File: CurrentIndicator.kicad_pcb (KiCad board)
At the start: 2 copper layers, 60 x 100 mm, 79 parts, among them J1 Conn_01x02_Male, J2 Conn_01x04_Male, J3 Conn_01x04_Male, J6 Micro_SD_Card_Det, J7 USB_B_Micro, Q1 IRLML6344TRPBFTR, Q2 IRLML6344TRPBFTR, Q3 IRLML6344TRPBFTR, Q4 IRLML6344TRPBFTR, SW1 TVAF06-A020B-R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

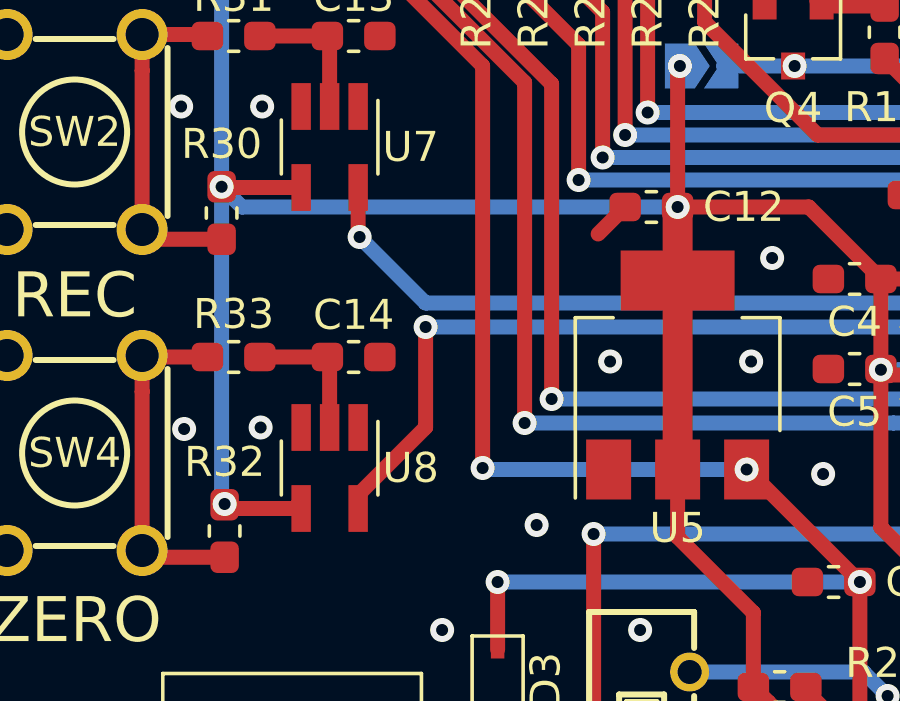
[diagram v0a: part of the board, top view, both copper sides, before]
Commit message: シュミットトリガのピン配置修正
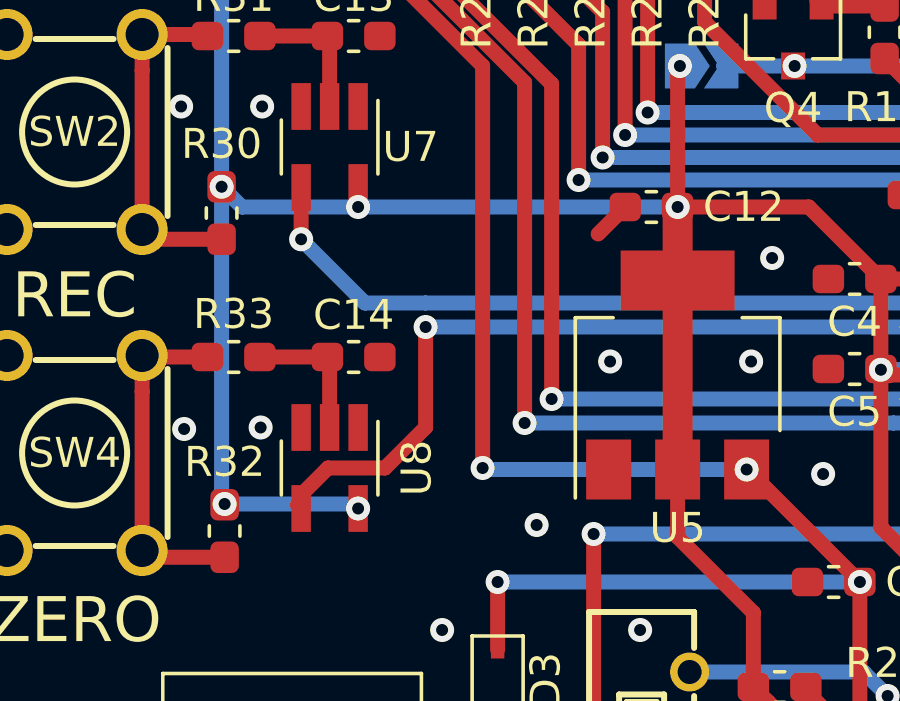
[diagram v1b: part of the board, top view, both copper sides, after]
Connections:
- U7 pad 4: +3V3 -> /REC_SW
- U7 pad 5: /REC_SW -> +3V3
- U8 pad 4: +3V3 -> /OFFSET_SW
- U8 pad 5: /OFFSET_SW -> +3V3
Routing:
- net /OFFSET_SW: track 25.6 -> 27.7 mm
- net /REC_SW: track 23.4 -> 25.4 mm
- net +3V3: track 225.5 -> 225.9 mm, vias 9 -> 11
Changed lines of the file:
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@@
     (thickness 1.6)
     (drawings 28)
-    (tracks 456)
+    (tracks 463)
     (zones 0)
     (modules 79)
@@
   )
   (setup
-    (last_trace_width 0.25)
+    (last_trace_width 0.5)
     (user_trace_width 0.5)
     (user_trace_width 1)
@@
     (add_net "Net-(J6-Pad11)")
     (add_net "Net-(J6-Pad8)")
+    (add_net "Net-(J7-Pad4)")
     (add_net "Net-(JP1-Pad2)")
     (add_net "Net-(Q1-Pad1)")
@@
     (add_net "Net-(R32-Pad2)")
     (add_net "Net-(R7-Pad1)")
+    (add_net "Net-(U2-Pad14)")
+    (add_net "Net-(U2-Pad15)")
+    (add_net "Net-(U2-Pad16)")
     (add_net "Net-(U2-Pad2)")
+    (add_net "Net-(U2-Pad7)")
+    (add_net "Net-(U7-Pad1)")
+    (add_net "Net-(U8-Pad1)")
+  )
+  (module Package_TO_SOT_SMD:SOT-23-5_HandSoldering (layer F.Cu)
+    (at 153 118.7 270)
+    (descr "5-pin SOT23 package")
+    (tags "SOT-23-5 hand-soldering")
+    (attr smd)
+    (fp_text reference U8 (at 0 -2.9 90) (layer F.SilkS)
+      (effects (font (size 1 1) (thickness 0.15)))
+    )
+    (fp_text value TC7S14F (at 0 2.9 90) (layer F.Fab)
+      (effects (font (size 1 1) (thickness 0.15)))
+    )
+    (fp_line (start 2.38 1.8) (end -2.38 1.8) (layer F.CrtYd) (width 0.05))
+    (fp_line (start 2.38 1.8) (end 2.38 -1.8) (layer F.CrtYd) (width 0.05))
+    (fp_line (start -2.38 -1.8) (end -2.38 1.8) (layer F.CrtYd) (width 0.05))
+    (fp_line (start -2.38 -1.8) (end 2.38 -1.8) (layer F.CrtYd) (width 0.05))
+    (fp_line (start 0.9 -1.55) (end 0.9 1.55) (layer F.Fab) (width 0.1))
+    (fp_line (start 0.9 1.55) (end -0.9 1.55) (layer F.Fab) (width 0.1))
+    (fp_line (start -0.9 -0.9) (end -0.9 1.55) (layer F.Fab) (width 0.1))
+    (fp_line (start 0.9 -1.55) (end -0.25 -1.55) (layer F.Fab) (width 0.1))
+    (fp_line (start -0.9 -0.9) (end -0.25 -1.55) (layer F.Fab) (width 0.1))
+    (fp_line (start 0.9 -1.61) (end -1.55 -1.61) (layer F.SilkS) (width 0.12))
+    (fp_line (start -0.9 1.61) (end 0.9 1.61) (layer F.SilkS) (width 0.12))
+    (fp_text user %R (at 0 0) (layer F.Fab)
+      (effects (font (size 0.5 0.5) (thickness 0.075)))
+    )
+    (pad 5 smd rect (at 1.35 -0.95 270) (size 1.56 0.65) (layers F.Cu F.Paste F.Mask)
+      (net 2 +3V3))
+    (pad 4 smd rect (at 1.35 0.95 270) (size 1.56 0.65) (layers F.Cu F.Paste F.Mask)
+      (net 66 /OFFSET_SW))
+    (pad 3 smd rect (at -1.35 0.95 270) (size 1.56 0.65) (layers F.Cu F.Paste F.Mask)
+      (net 1 GND))
+    (pad 2 smd rect (at -1.35 0 270) (size 1.56 0.65) (layers F.Cu F.Paste F.Mask)
+      (net 9 "Net-(C14-Pad1)"))
+    (pad 1 smd rect (at -1.35 -0.95 270) (size 1.56 0.65) (layers F.Cu F.Paste F.Mask))
+    (model ${KISYS3DMOD}/Package_TO_SOT_SMD.3dshapes/SOT-23-5.wrl
+      (at (xyz 0 0 0))
+      (scale (xyz 1 1 1))
+      (rotate (xyz 0 0 0))
+    )
   )
   (module Capacitor_SMD:C_0603_1608Metric_Pad1.05x0.95mm_HandSolder (layer F.Cu)
@@
   )
   (module Package_TO_SOT_SMD:SOT-23-5_HandSoldering (layer F.Cu)
-    (at 153 118.7 270)
-    (descr "5-pin SOT23 package")
-    (tags "SOT-23-5 hand-soldering")
-    (attr smd)
-    (fp_text reference U8 (at 0 -2.7 180) (layer F.SilkS)
-      (effects (font (size 1 1) (thickness 0.15)))
-    )
-    (fp_text value TC7S14F (at 0 2.9 90) (layer F.Fab)
-      (effects (font (size 1 1) (thickness 0.15)))
-    )
-    (fp_line (start 2.38 1.8) (end -2.38 1.8) (layer F.CrtYd) (width 0.05))
-    (fp_line (start 2.38 1.8) (end 2.38 -1.8) (layer F.CrtYd) (width 0.05))
-    (fp_line (start -2.38 -1.8) (end -2.38 1.8) (layer F.CrtYd) (width 0.05))
-    (fp_line (start -2.38 -1.8) (end 2.38 -1.8) (layer F.CrtYd) (width 0.05))
-    (fp_line (start 0.9 -1.55) (end 0.9 1.55) (layer F.Fab) (width 0.1))
-    (fp_line (start 0.9 1.55) (end -0.9 1.55) (layer F.Fab) (width 0.1))
-    (fp_line (start -0.9 -0.9) (end -0.9 1.55) (layer F.Fab) (width 0.1))
-    (fp_line (start 0.9 -1.55) (end -0.25 -1.55) (layer F.Fab) (width 0.1))
-    (fp_line (start -0.9 -0.9) (end -0.25 -1.55) (layer F.Fab) (width 0.1))
-    (fp_line (start 0.9 -1.61) (end -1.55 -1.61) (layer F.SilkS) (width 0.12))
-    (fp_line (start -0.9 1.61) (end 0.9 1.61) (layer F.SilkS) (width 0.12))
-    (fp_text user %R (at 0 0) (layer F.Fab)
-      (effects (font (size 0.5 0.5) (thickness 0.075)))
-    )
-    (pad 5 smd rect (at 1.35 -0.95 270) (size 1.56 0.65) (layers F.Cu F.Paste F.Mask)
-      (net 66 /OFFSET_SW))
-    (pad 4 smd rect (at 1.35 0.95 270) (size 1.56 0.65) (layers F.Cu F.Paste F.Mask)
-      (net 2 +3V3))
-    (pad 3 smd rect (at -1.35 0.95 270) (size 1.56 0.65) (layers F.Cu F.Paste F.Mask)
-      (net 1 GND))
-    (pad 2 smd rect (at -1.35 0 270) (size 1.56 0.65) (layers F.Cu F.Paste F.Mask)
-      (net 9 "Net-(C14-Pad1)"))
-    (pad 1 smd rect (at -1.35 -0.95 270) (size 1.56 0.65) (layers F.Cu F.Paste F.Mask))
-    (model ${KISYS3DMOD}/Package_TO_SOT_SMD.3dshapes/SOT-23-5.wrl
-      (at (xyz 0 0 0))
-      (scale (xyz 1 1 1))
-      (rotate (xyz 0 0 0))
-    )
-  )
-  (module Package_TO_SOT_SMD:SOT-23-5_HandSoldering (layer F.Cu)
     (at 153 108 270)
     (descr "5-pin SOT23 package")
@@
     )
     (pad 5 smd rect (at 1.35 -0.95 270) (size 1.56 0.65) (layers F.Cu F.Paste F.Mask)
-      (net 67 /REC_SW))
-    (pad 4 smd rect (at 1.35 0.95 270) (size 1.56 0.65) (layers F.Cu F.Paste F.Mask)
       (net 2 +3V3))
+    (pad 4 smd rect (at 1.35 0.95 270) (size 1.56 0.65) (layers F.Cu F.Paste F.Mask)
+      (net 67 /REC_SW))
     (pad 3 smd rect (at -1.35 0.95 270) (size 1.56 0.65) (layers F.Cu F.Paste F.Mask)
       (net 1 GND))
@@
   (segment (start 171.375 115.6) (end 171.375 115.6) (width 0.5) (layer F.Cu) (net 2))
   (segment (start 171.375 112.4) (end 171.375 115.425) (width 0.5) (layer F.Cu) (net 2))
-  (segment (start 152.05 109.35) (end 149.425 109.35) (width 0.5) (layer F.Cu) (net 2))
-  (segment (start 151.925 119.925) (end 152.05 120.05) (width 0.5) (layer F.Cu) (net 2))
+  (segment (start 151.925 119.925) (end 152.05 120.05) (width 0.5) (layer F.Cu) (net 66))
   (segment (start 176.925 128.5) (end 176.9 128.525) (width 0.5) (layer F.Cu) (net 2))
   (segment (start 183 128.5) (end 176.925 128.5) (width 0.5) (layer F.Cu) (net 2))
@@
   (segment (start 164.6 105.375) (end 164.675 105.3) (width 0.5) (layer B.Cu) (net 2))
   (segment (start 150.075 110) (end 149.4 109.325) (width 0.5) (layer B.Cu) (net 2))
-  (segment (start 164.6 110) (end 150.075 110) (width 0.5) (layer B.Cu) (net 2))
+  (segment (start 164.6 110) (end 153.95 110) (width 0.5) (layer B.Cu) (net 2))
   (via (at 163.4 134.1) (size 0.8) (drill 0.4) (layers F.Cu B.Cu) (net 2))
   (segment (start 163.4 136.6475) (end 163.4 134.1) (width 0.5) (layer F.Cu) (net 2))
@@
   (segment (start 163.4 134.1) (end 167.125 134.1) (width 0.5) (layer B.Cu) (net 2))
   (segment (start 173.925 126.3) (end 176.925 126.3) (width 0.5) (layer F.Cu) (net 2))
-  (segment (start 152.05 120.05) (end 149.65 120.05) (width 0.5) (layer F.Cu) (net 2))
   (via (at 164.675 105.3) (size 0.8) (drill 0.4) (layers F.Cu B.Cu) (net 2))
   (segment (start 164.6 110) (end 164.6 105.375) (width 0.5) (layer F.Cu) (net 2))
@@
   (via (at 156.2 114) (size 0.8) (drill 0.4) (layers F.Cu B.Cu) (net 66))
   (segment (start 156.2 117.345) (end 156.2 114) (width 0.5) (layer F.Cu) (net 66))
-  (segment (start 153.95 120.05) (end 153.95 119.595) (width 0.5) (layer F.Cu) (net 66))
-  (segment (start 153.95 119.595) (end 156.2 117.345) (width 0.5) (layer F.Cu) (net 66))
+  (segment (start 153.95 120.05) (end 153.95 119.595) (width 0.5) (layer F.Cu) (net 2))
+  (segment (start 153.95 110) (end 150.075 110) (width 0.5) (layer B.Cu) (net 2))
+  (via (at 153.95 110) (size 0.8) (drill 0.4) (layers F.Cu B.Cu) (net 2))
+  (segment (start 153.95 110) (end 153.95 109.35) (width 0.5) (layer F.Cu) (net 2))
+  (via (at 153.95 120.05) (size 0.8) (drill 0.4) (layers F.Cu B.Cu) (net 2))
+  (segment (start 149.5 119.9) (end 153.8 119.9) (width 0.5) (layer B.Cu) (net 2))
+  (segment (start 153.8 119.9) (end 153.95 120.05) (width 0.5) (layer B.Cu) (net 2))
   (segment (start 172.4 114) (end 156.2 114) (width 0.5) (layer B.Cu) (net 66))
+  (segment (start 152.05 119.595) (end 152.945 118.7) (width 0.5) (layer F.Cu) (net 66))
+  (segment (start 152.05 120.05) (end 152.05 119.595) (width 0.5) (layer F.Cu) (net 66))
+  (segment (start 154.845 118.7) (end 156.2 117.345) (width 0.5) (layer F.Cu) (net 66))
+  (segment (start 152.945 118.7) (end 154.845 118.7) (width 0.5) (layer F.Cu) (net 66))
   (via (at 173.3 113.2) (size 0.8) (drill 0.4) (layers F.Cu B.Cu) (net 67))
   (segment (start 174.825 113.2) (end 173.3 113.2) (width 0.5) (layer F.Cu) (net 67))
-  (via (at 154 111) (size 0.8) (drill 0.4) (layers F.Cu B.Cu) (net 67))
   (segment (start 173.3 113.2) (end 156.2 113.2) (width 0.5) (layer B.Cu) (net 67))
-  (segment (start 156.2 113.2) (end 154 111) (width 0.5) (layer B.Cu) (net 67))
-  (segment (start 153.95 110.95) (end 154 111) (width 0.5) (layer F.Cu) (net 67))
-  (segment (start 153.95 109.35) (end 153.95 110.95) (width 0.5) (layer F.Cu) (net 67))
+  (via (at 152.05 111.075) (size 0.8) (drill 0.4) (layers F.Cu B.Cu) (net 67))
+  (segment (start 156.2 113.2) (end 154.175 113.2) (width 0.5) (layer B.Cu) (net 67))
+  (segment (start 154.175 113.2) (end 152.05 111.075) (width 0.5) (layer B.Cu) (net 67))
+  (segment (start 152.05 111.075) (end 152.05 109.35) (width 0.5) (layer F.Cu) (net 67))
   (zone (net 0) (net_name "") (layer F.Cu) (hatch edge 0.508)
     (connect_pads (clearance 0.508))
@@
     (polygon
       (pts
-        (xy 156.85 117.5) (xy 157.4 117.5) (xy 157.1 117.15)
+        (xy 156.923568 117.575) (xy 157.473568 119.425) (xy 154.923568 119.425)
       )
     )
